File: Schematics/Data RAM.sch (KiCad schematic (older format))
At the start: 9 parts, among them U10 74LS32, U11 74LS04, U12 IDT71256SA12TPG, U13 IDT71256SA12TPG, U9 74LS32

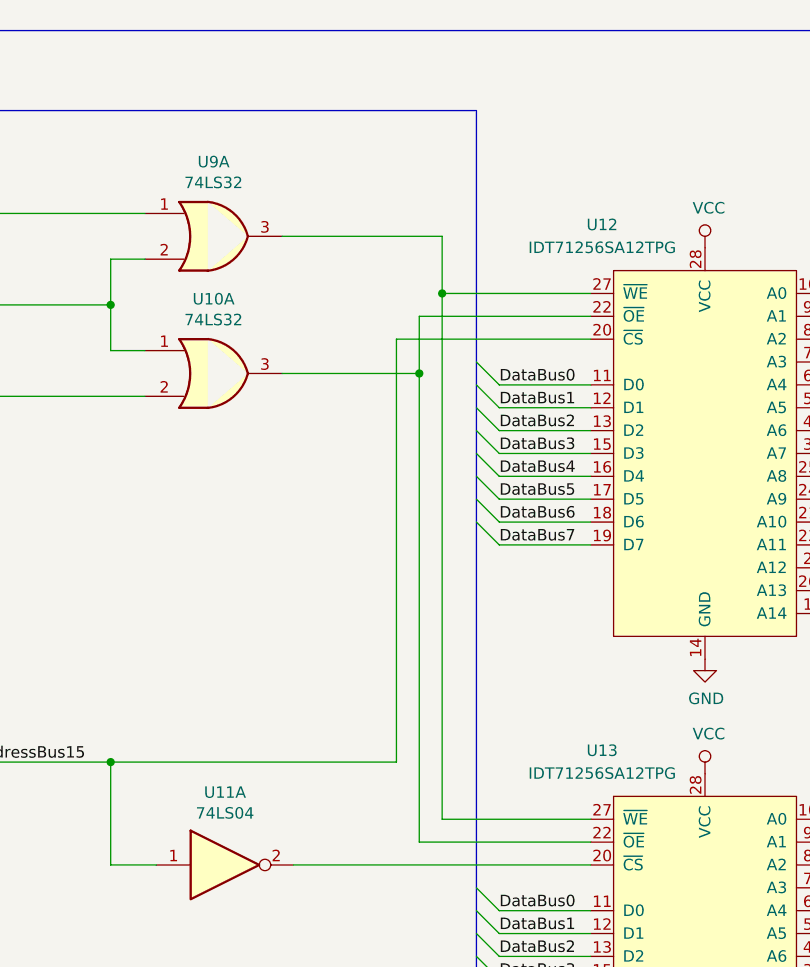
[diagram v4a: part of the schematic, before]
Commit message: Add unused IC units to Output Display to ensure no ICs are shared with other modules.
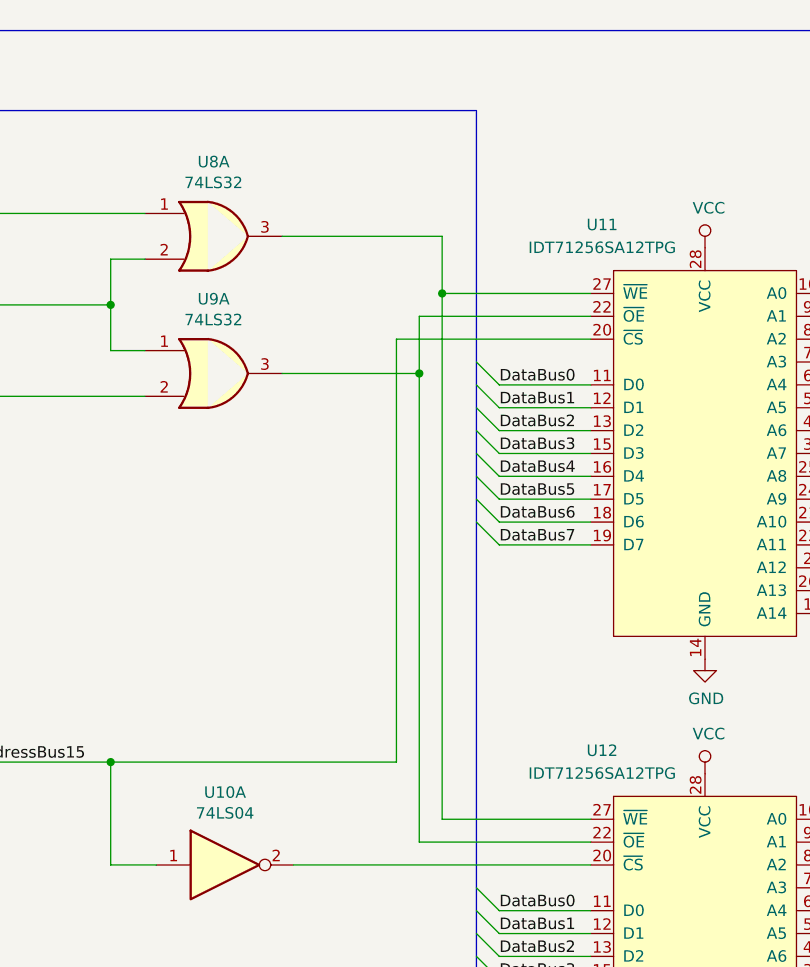
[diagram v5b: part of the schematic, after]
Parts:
- renumbered U11 to U10, U12 to U11, U13 to U12, U9 to U8, U10 to U9
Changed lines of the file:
@@
 $EndDescr
 $Comp
-L Memory_RAM:IDT71256SA12TPG U12
+L Memory_RAM:IDT71256SA12TPG U11
 U 1 1 5E1E9FA0
 P 6850 2700
-F 0 "U12" H 6400 3650 50  0000 C CNN
+F 0 "U11" H 6400 3650 50  0000 C CNN
 F 1 "IDT71256SA12TPG" H 6400 3550 50  0000 C CNN
 F 2 "Package_DIP:DIP-28_W7.62mm_Socket" H 6850 4700 50  0001 C CNN
@@
 $EndComp
 $Comp
-L Memory_RAM:IDT71256SA12TPG U13
+L Memory_RAM:IDT71256SA12TPG U12
 U 1 1 5E1EC273
 P 6850 5000
-F 0 "U13" H 6400 5950 50  0000 C CNN
+F 0 "U12" H 6400 5950 50  0000 C CNN
 F 1 "IDT71256SA12TPG" H 6400 5850 50  0000 C CNN
 F 2 "Package_DIP:DIP-28_W7.62mm_Socket" H 6850 7000 50  0001 C CNN
@@
 $EndComp
 $Comp
-L power:GND #PWR0116
+L power:GND #PWR019
 U 1 1 5E1EE0BF
 P 6850 3650
-F 0 "#PWR0116" H 6850 3400 50  0001 C CNN
+F 0 "#PWR019" H 6850 3400 50  0001 C CNN
 F 1 "GND" H 6855 3477 50  0000 C CNN
 F 2 "" H 6850 3650 50  0001 C CNN
@@
 $EndComp
 $Comp
-L power:GND #PWR0117
+L power:GND #PWR021
 U 1 1 5E1EE650
 P 6850 5950
-F 0 "#PWR0117" H 6850 5700 50  0001 C CNN
+F 0 "#PWR021" H 6850 5700 50  0001 C CNN
 F 1 "GND" H 6855 5777 50  0000 C CNN
 F 2 "" H 6850 5950 50  0001 C CNN
@@
 $EndComp
 $Comp
-L power:VCC #PWR0118
+L power:VCC #PWR020
 U 1 1 5E1EEC64
 P 6850 4150
-F 0 "#PWR0118" H 6850 4000 50  0001 C CNN
+F 0 "#PWR020" H 6850 4000 50  0001 C CNN
 F 1 "VCC" H 6867 4323 50  0000 C CNN
 F 2 "" H 6850 4150 50  0001 C CNN
@@
 $EndComp
 $Comp
-L power:VCC #PWR0119
+L power:VCC #PWR018
 U 1 1 5E1EF332
 P 6850 1850
-F 0 "#PWR0119" H 6850 1700 50  0001 C CNN
+F 0 "#PWR018" H 6850 1700 50  0001 C CNN
 F 1 "VCC" H 6867 2023 50  0000 C CNN
 F 2 "" H 6850 1850 50  0001 C CNN
@@
 P 4700 2400
 AR Path="/5D2C0C74/5E2163C3" Ref="U?"  Part="1"
-AR Path="/5D2C1188/5E2163C3" Ref="U10"  Part="1"
-F 0 "U10" H 4700 2725 50  0000 C CNN
+AR Path="/5D2C1188/5E2163C3" Ref="U9"  Part="1"
+F 0 "U9" H 4700 2725 50  0000 C CNN
 F 1 "74LS32" H 4700 2634 50  0000 C CNN
 F 2 "Package_DIP:DIP-14_W7.62mm" H 4700 2400 50  0001 C CNN
@@
 P 4700 1800
 AR Path="/5D2C0C74/5E2163CE" Ref="U?"  Part="1"
-AR Path="/5D2C1188/5E2163CE" Ref="U9"  Part="1"
-F 0 "U9" H 4700 2125 50  0000 C CNN
+AR Path="/5D2C1188/5E2163CE" Ref="U8"  Part="1"
+F 0 "U8" H 4700 2125 50  0000 C CNN
 F 1 "74LS32" H 4700 2034 50  0000 C CNN
 F 2 "Package_DIP:DIP-14_W7.62mm" H 4700 1800 50  0001 C CNN
@@
 Connection ~ 5600 2400
 $Comp
-L 74xx:74LS04 U11
+L 74xx:74LS04 U10
 U 1 1 5E2339CC
 P 4750 4550
-F 0 "U11" H 4750 4867 50  0000 C CNN
+F 0 "U10" H 4750 4867 50  0000 C CNN
 F 1 "74LS04" H 4750 4776 50  0000 C CNN
 F 2 "Package_DIP:DIP-14_W7.62mm" H 4750 4550 50  0001 C CNN
@@
 P 800 7750
 AR Path="/5D2C07CD/5E26225F" Ref="#PWR?"  Part="1"
-AR Path="/5D2C1188/5E26225F" Ref="#PWR0120"  Part="1"
-F 0 "#PWR0120" H 800 7500 50  0001 C CNN
+AR Path="/5D2C1188/5E26225F" Ref="#PWR017"  Part="1"
+F 0 "#PWR017" H 800 7500 50  0001 C CNN
 F 1 "GND" H 805 7577 50  0000 C CNN
 F 2 "" H 800 7750 50  0001 C CNN
@@
 P 800 7450
 AR Path="/5D2C07CD/5E262265" Ref="#PWR?"  Part="1"
-AR Path="/5D2C1188/5E262265" Ref="#PWR0121"  Part="1"
-F 0 "#PWR0121" H 800 7300 50  0001 C CNN
+AR Path="/5D2C1188/5E262265" Ref="#PWR016"  Part="1"
+F 0 "#PWR016" H 800 7300 50  0001 C CNN
 F 1 "VCC" H 817 7623 50  0000 C CNN
 F 2 "" H 800 7450 50  0001 C CNN

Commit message: Add unused IC units to Data RAM to ensure no ICs are shared with other modules.
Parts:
- added unit 3 of U8
- added unit 4 of U8
- added unit 2 of U9
- added unit 4 of U9
- added unit 3 of U9
- added unit 5 of U9
- added unit 6 of U9
- renumbered U11 to U10, U12 to U11, U9 to U8, U10 to U9
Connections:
- net DeviceSelect5: now also U8.4; no longer U8.1
- net ~MO: now also U8.5; no longer U8.2
- net at U10.22 (~OE), U11.22 (~OE): now also U8.6; no longer U8.3
- no-connect marks 0 -> 16
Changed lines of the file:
@@
 $EndDescr
 $Comp
-L Memory_RAM:IDT71256SA12TPG U11
+L Memory_RAM:IDT71256SA12TPG U10
 U 1 1 5E1E9FA0
 P 6850 2700
-F 0 "U11" H 6400 3650 50  0000 C CNN
+F 0 "U10" H 6400 3650 50  0000 C CNN
 F 1 "IDT71256SA12TPG" H 6400 3550 50  0000 C CNN
 F 2 "Package_DIP:DIP-28_W7.62mm_Socket" H 6850 4700 50  0001 C CNN
@@
 $EndComp
 $Comp
-L Memory_RAM:IDT71256SA12TPG U12
+L Memory_RAM:IDT71256SA12TPG U11
 U 1 1 5E1EC273
 P 6850 5000
-F 0 "U12" H 6400 5950 50  0000 C CNN
+F 0 "U11" H 6400 5950 50  0000 C CNN
 F 1 "IDT71256SA12TPG" H 6400 5850 50  0000 C CNN
 F 2 "Package_DIP:DIP-28_W7.62mm_Socket" H 6850 7000 50  0001 C CNN
@@
 $Comp
 L 74xx:74LS32 U?
-U 1 1 5E2163C3
+U 2 1 5E2163C3
 P 4700 2400
 AR Path="/5D2C0C74/5E2163C3" Ref="U?"  Part="1"
-AR Path="/5D2C1188/5E2163C3" Ref="U9"  Part="1"
-F 0 "U9" H 4700 2725 50  0000 C CNN
+AR Path="/5D2C1188/5E2163C3" Ref="U8"  Part="2"
+F 0 "U8" H 4700 2725 50  0000 C CNN
 F 1 "74LS32" H 4700 2634 50  0000 C CNN
 F 2 "Package_DIP:DIP-14_W7.62mm" H 4700 2400 50  0001 C CNN
 F 3 "http://www.ti.com/lit/gpn/sn74LS32" H 4700 2400 50  0001 C CNN
-	1    4700 2400
+	2    4700 2400
 	1    0    0    -1
 $EndComp
@@
 Connection ~ 5600 2400
 $Comp
-L 74xx:74LS04 U10
+L 74xx:74LS04 U9
 U 1 1 5E2339CC
 P 4750 4550
-F 0 "U10" H 4750 4867 50  0000 C CNN
+F 0 "U9" H 4750 4867 50  0000 C CNN
 F 1 "74LS04" H 4750 4776 50  0000 C CNN
 F 2 "Package_DIP:DIP-14_W7.62mm" H 4750 4550 50  0001 C CNN
@@
 Connection ~ 1300 7750
 Connection ~ 800  7750
+$Comp
+L 74xx:74LS32 U?
+U 3 1 5DB5AC2C
+P 1350 4650
+AR Path="/5D2C0C74/5DB5AC2C" Ref="U?"  Part="1"
+AR Path="/5D2C1188/5DB5AC2C" Ref="U8"  Part="3"
+F 0 "U8" H 1350 4975 50  0000 C CNN
+F 1 "74LS32" H 1350 4884 50  0000 C CNN
+F 2 "Package_DIP:DIP-14_W7.62mm" H 1350 4650 50  0001 C CNN
+F 3 "http://www.ti.com/lit/gpn/sn74LS32" H 1350 4650 50  0001 C CNN
+	3    1350 4650
+	1    0    0    -1
+$EndComp
+$Comp
+L 74xx:74LS32 U?
+U 4 1 5DB5BEE6
+P 1350 5200
+AR Path="/5D2C0C74/5DB5BEE6" Ref="U?"  Part="1"
+AR Path="/5D2C1188/5DB5BEE6" Ref="U8"  Part="4"
+F 0 "U8" H 1350 5525 50  0000 C CNN
+F 1 "74LS32" H 1350 5434 50  0000 C CNN
+F 2 "Package_DIP:DIP-14_W7.62mm" H 1350 5200 50  0001 C CNN
+F 3 "http://www.ti.com/lit/gpn/sn74LS32" H 1350 5200 50  0001 C CNN
+	4    1350 5200
+	1    0    0    -1
+$EndComp
+NoConn ~ 1050 4550
+NoConn ~ 1050 4750
+NoConn ~ 1050 5100
+NoConn ~ 1050 5300
+NoConn ~ 1650 5200
+NoConn ~ 1650 4650
+$Comp
+L 74xx:74LS04 U9
+U 4 1 5DB73163
+P 1350 6350
+F 0 "U9" H 1350 6667 50  0000 C CNN
+F 1 "74LS04" H 1350 6576 50  0000 C CNN
+F 2 "Package_DIP:DIP-14_W7.62mm" H 1350 6350 50  0001 C CNN
+F 3 "http://www.ti.com/lit/gpn/sn74LS04" H 1350 6350 50  0001 C CNN
+	4    1350 6350
+	1    0    0    -1
+$EndComp
+$Comp
+L 74xx:74LS04 U9
+U 3 1 5DB74AE3
+P 2050 5850
+F 0 "U9" H 2050 6167 50  0000 C CNN
+F 1 "74LS04" H 2050 6076 50  0000 C CNN
+F 2 "Package_DIP:DIP-14_W7.62mm" H 2050 5850 50  0001 C CNN
+F 3 "http://www.ti.com/lit/gpn/sn74LS04" H 2050 5850 50  0001 C CNN
+	3    2050 5850
+	1    0    0    -1
+$EndComp
+$Comp
+L 74xx:74LS04 U9
+U 5 1 5DB758F0
+P 2050 6350
+F 0 "U9" H 2050 6667 50  0000 C CNN
+F 1 "74LS04" H 2050 6576 50  0000 C CNN
+F 2 "Package_DIP:DIP-14_W7.62mm" H 2050 6350 50  0001 C CNN
+F 3 "http://www.ti.com/lit/gpn/sn74LS04" H 2050 6350 50  0001 C CNN
+	5    2050 6350
+	1    0    0    -1
+$EndComp
+$Comp
+L 74xx:74LS04 U9
+U 6 1 5DB7656E
+P 1350 6900
+F 0 "U9" H 1350 7217 50  0000 C CNN
+F 1 "74LS04" H 1350 7126 50  0000 C CNN
+F 2 "Package_DIP:DIP-14_W7.62mm" H 1350 6900 50  0001 C CNN
+F 3 "http://www.ti.com/lit/gpn/sn74LS04" H 1350 6900 50  0001 C CNN
+	6    1350 6900
+	1    0    0    -1
+$EndComp
+$Comp
+L 74xx:74LS04 U9
+U 2 1 5DB72272
+P 1350 5850
+F 0 "U9" H 1350 6167 50  0000 C CNN
+F 1 "74LS04" H 1350 6076 50  0000 C CNN
+F 2 "Package_DIP:DIP-14_W7.62mm" H 1350 5850 50  0001 C CNN
+F 3 "http://www.ti.com/lit/gpn/sn74LS04" H 1350 5850 50  0001 C CNN
+	2    1350 5850
+	1    0    0    -1
+$EndComp
+NoConn ~ 1050 5850
+NoConn ~ 1050 6350
+NoConn ~ 1050 6900
+NoConn ~ 1650 6900
+NoConn ~ 1650 6350
+NoConn ~ 1650 5850
+NoConn ~ 1750 5850
+NoConn ~ 1750 6350
+NoConn ~ 2350 6350
+NoConn ~ 2350 5850
 Wire Bus Line
 	5850 1250 5850 5350

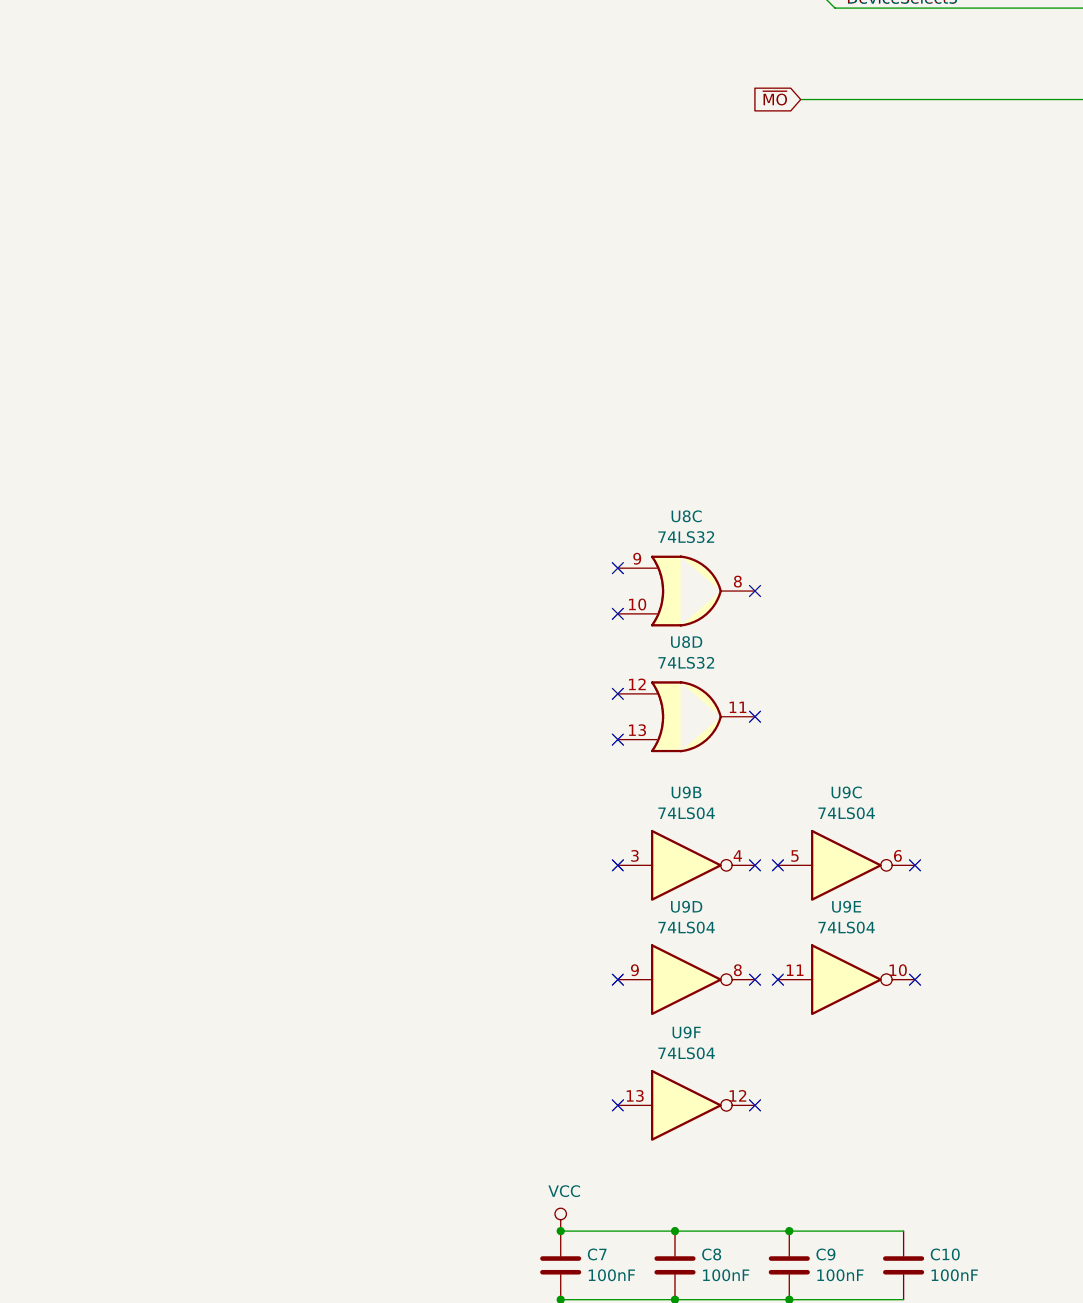
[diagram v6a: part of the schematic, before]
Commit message: Change assignment of logic units to reduce the number of discrete ICs.
This reduces part count in the Instruction RAM module.
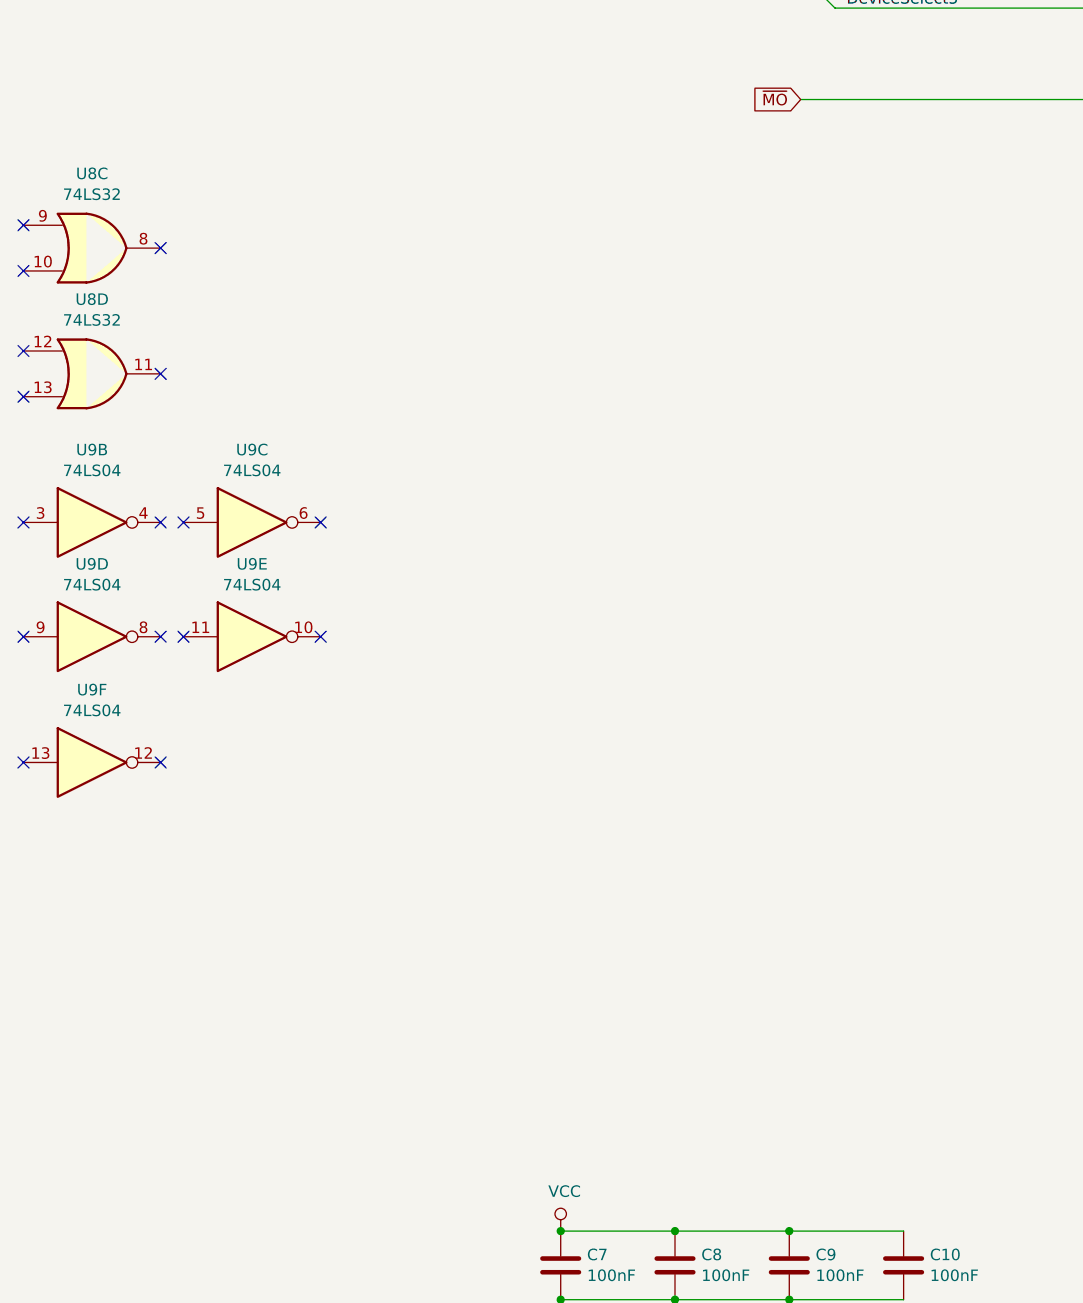
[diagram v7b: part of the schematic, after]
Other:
- moved on the sheet: U8C, U8D, U9B, U9C, U9D, U9E, U9F
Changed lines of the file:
@@
 $Descr USLetter 11000 8500
 encoding utf-8
-Sheet 3 24
+Sheet 3 22
 Title "Data RAM"
 Date ""
@@
 L 74xx:74LS32 U?
 U 3 1 5DB5AC2C
-P 1350 4650
+P -1250 3150
 AR Path="/5D2C0C74/5DB5AC2C" Ref="U?"  Part="1"
 AR Path="/5D2C1188/5DB5AC2C" Ref="U8"  Part="3"
-F 0 "U8" H 1350 4975 50  0000 C CNN
-F 1 "74LS32" H 1350 4884 50  0000 C CNN
-F 2 "Package_DIP:DIP-14_W7.62mm" H 1350 4650 50  0001 C CNN
-F 3 "http://www.ti.com/lit/gpn/sn74LS32" H 1350 4650 50  0001 C CNN
-	3    1350 4650
+F 0 "U8" H -1250 3475 50  0000 C CNN
+F 1 "74LS32" H -1250 3384 50  0000 C CNN
+F 2 "Package_DIP:DIP-14_W7.62mm" H -1250 3150 50  0001 C CNN
+F 3 "http://www.ti.com/lit/gpn/sn74LS32" H -1250 3150 50  0001 C CNN
+	3    -1250 3150
 	1    0    0    -1
 $EndComp
@@
 L 74xx:74LS32 U?
 U 4 1 5DB5BEE6
-P 1350 5200
+P -1250 3700
 AR Path="/5D2C0C74/5DB5BEE6" Ref="U?"  Part="1"
 AR Path="/5D2C1188/5DB5BEE6" Ref="U8"  Part="4"
-F 0 "U8" H 1350 5525 50  0000 C CNN
-F 1 "74LS32" H 1350 5434 50  0000 C CNN
-F 2 "Package_DIP:DIP-14_W7.62mm" H 1350 5200 50  0001 C CNN
-F 3 "http://www.ti.com/lit/gpn/sn74LS32" H 1350 5200 50  0001 C CNN
-	4    1350 5200
-	1    0    0    -1
-$EndComp
-NoConn ~ 1050 4550
-NoConn ~ 1050 4750
-NoConn ~ 1050 5100
-NoConn ~ 1050 5300
-NoConn ~ 1650 5200
-NoConn ~ 1650 4650
+F 0 "U8" H -1250 4025 50  0000 C CNN
+F 1 "74LS32" H -1250 3934 50  0000 C CNN
+F 2 "Package_DIP:DIP-14_W7.62mm" H -1250 3700 50  0001 C CNN
+F 3 "http://www.ti.com/lit/gpn/sn74LS32" H -1250 3700 50  0001 C CNN
+	4    -1250 3700
+	1    0    0    -1
+$EndComp
+NoConn ~ -1550 3050
+NoConn ~ -1550 3250
+NoConn ~ -1550 3600
+NoConn ~ -1550 3800
+NoConn ~ -950 3700
+NoConn ~ -950 3150
 $Comp
 L 74xx:74LS04 U9
 U 4 1 5DB73163
-P 1350 6350
-F 0 "U9" H 1350 6667 50  0000 C CNN
-F 1 "74LS04" H 1350 6576 50  0000 C CNN
-F 2 "Package_DIP:DIP-14_W7.62mm" H 1350 6350 50  0001 C CNN
-F 3 "http://www.ti.com/lit/gpn/sn74LS04" H 1350 6350 50  0001 C CNN
-	4    1350 6350
+P -1250 4850
+F 0 "U9" H -1250 5167 50  0000 C CNN
+F 1 "74LS04" H -1250 5076 50  0000 C CNN
+F 2 "Package_DIP:DIP-14_W7.62mm" H -1250 4850 50  0001 C CNN
+F 3 "http://www.ti.com/lit/gpn/sn74LS04" H -1250 4850 50  0001 C CNN
+	4    -1250 4850
 	1    0    0    -1
 $EndComp
@@
 L 74xx:74LS04 U9
 U 3 1 5DB74AE3
-P 2050 5850
-F 0 "U9" H 2050 6167 50  0000 C CNN
-F 1 "74LS04" H 2050 6076 50  0000 C CNN
-F 2 "Package_DIP:DIP-14_W7.62mm" H 2050 5850 50  0001 C CNN
-F 3 "http://www.ti.com/lit/gpn/sn74LS04" H 2050 5850 50  0001 C CNN
-	3    2050 5850
+P -550 4350
+F 0 "U9" H -550 4667 50  0000 C CNN
+F 1 "74LS04" H -550 4576 50  0000 C CNN
+F 2 "Package_DIP:DIP-14_W7.62mm" H -550 4350 50  0001 C CNN
+F 3 "http://www.ti.com/lit/gpn/sn74LS04" H -550 4350 50  0001 C CNN
+	3    -550 4350
 	1    0    0    -1
 $EndComp
@@
 L 74xx:74LS04 U9
 U 5 1 5DB758F0
-P 2050 6350
-F 0 "U9" H 2050 6667 50  0000 C CNN
-F 1 "74LS04" H 2050 6576 50  0000 C CNN
-F 2 "Package_DIP:DIP-14_W7.62mm" H 2050 6350 50  0001 C CNN
-F 3 "http://www.ti.com/lit/gpn/sn74LS04" H 2050 6350 50  0001 C CNN
-	5    2050 6350
+P -550 4850
+F 0 "U9" H -550 5167 50  0000 C CNN
+F 1 "74LS04" H -550 5076 50  0000 C CNN
+F 2 "Package_DIP:DIP-14_W7.62mm" H -550 4850 50  0001 C CNN
+F 3 "http://www.ti.com/lit/gpn/sn74LS04" H -550 4850 50  0001 C CNN
+	5    -550 4850
 	1    0    0    -1
 $EndComp
@@
 L 74xx:74LS04 U9
 U 6 1 5DB7656E
-P 1350 6900
-F 0 "U9" H 1350 7217 50  0000 C CNN
-F 1 "74LS04" H 1350 7126 50  0000 C CNN
-F 2 "Package_DIP:DIP-14_W7.62mm" H 1350 6900 50  0001 C CNN
-F 3 "http://www.ti.com/lit/gpn/sn74LS04" H 1350 6900 50  0001 C CNN
-	6    1350 6900
+P -1250 5400
+F 0 "U9" H -1250 5717 50  0000 C CNN
+F 1 "74LS04" H -1250 5626 50  0000 C CNN
+F 2 "Package_DIP:DIP-14_W7.62mm" H -1250 5400 50  0001 C CNN
+F 3 "http://www.ti.com/lit/gpn/sn74LS04" H -1250 5400 50  0001 C CNN
+	6    -1250 5400
 	1    0    0    -1
 $EndComp
@@
 L 74xx:74LS04 U9
 U 2 1 5DB72272
-P 1350 5850
-F 0 "U9" H 1350 6167 50  0000 C CNN
-F 1 "74LS04" H 1350 6076 50  0000 C CNN
-F 2 "Package_DIP:DIP-14_W7.62mm" H 1350 5850 50  0001 C CNN
-F 3 "http://www.ti.com/lit/gpn/sn74LS04" H 1350 5850 50  0001 C CNN
-	2    1350 5850
-	1    0    0    -1
-$EndComp
-NoConn ~ 1050 5850
-NoConn ~ 1050 6350
-NoConn ~ 1050 6900
-NoConn ~ 1650 6900
-NoConn ~ 1650 6350
-NoConn ~ 1650 5850
-NoConn ~ 1750 5850
-NoConn ~ 1750 6350
-NoConn ~ 2350 6350
-NoConn ~ 2350 5850
+P -1250 4350
+F 0 "U9" H -1250 4667 50  0000 C CNN
+F 1 "74LS04" H -1250 4576 50  0000 C CNN
+F 2 "Package_DIP:DIP-14_W7.62mm" H -1250 4350 50  0001 C CNN
+F 3 "http://www.ti.com/lit/gpn/sn74LS04" H -1250 4350 50  0001 C CNN
+	2    -1250 4350
+	1    0    0    -1
+$EndComp
+NoConn ~ -1550 4350
+NoConn ~ -1550 4850
+NoConn ~ -1550 5400
+NoConn ~ -950 5400
+NoConn ~ -950 4850
+NoConn ~ -950 4350
+NoConn ~ -850 4350
+NoConn ~ -850 4850
+NoConn ~ -250 4850
+NoConn ~ -250 4350
 Wire Bus Line
 	5850 1250 5850 5350
